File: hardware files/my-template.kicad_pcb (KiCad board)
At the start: 2 copper layers, 17.5 x 24.7 mm, 23 parts, among them IC1 AD8232ACPZ-R7, J1 Conn_01x09

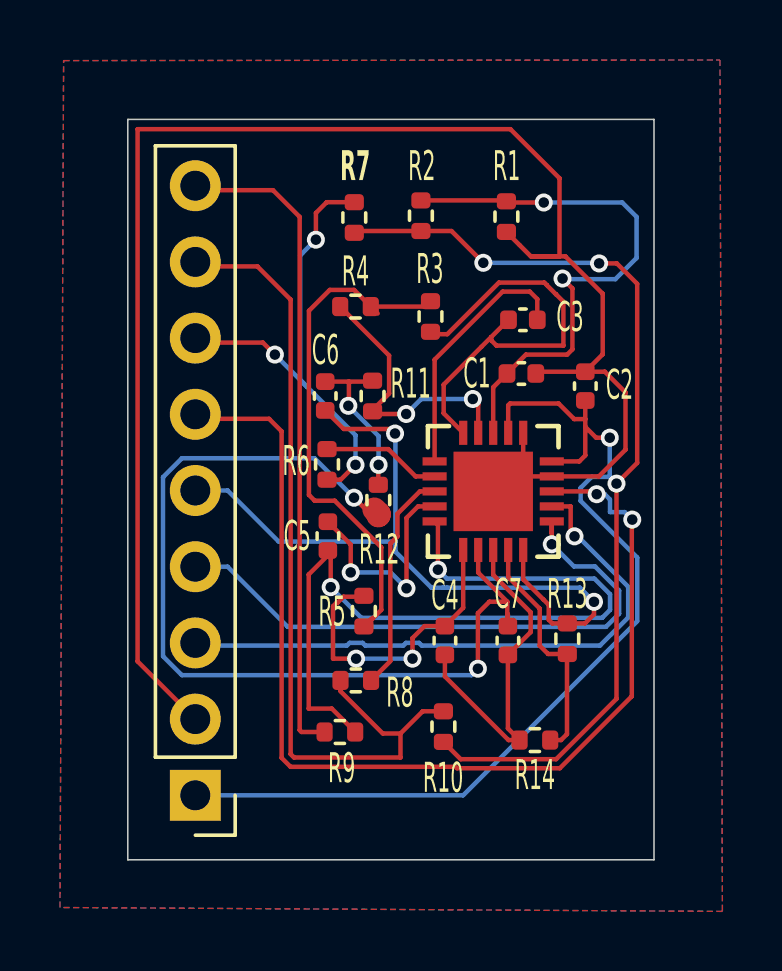
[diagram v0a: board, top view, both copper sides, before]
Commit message: update labels in pcb
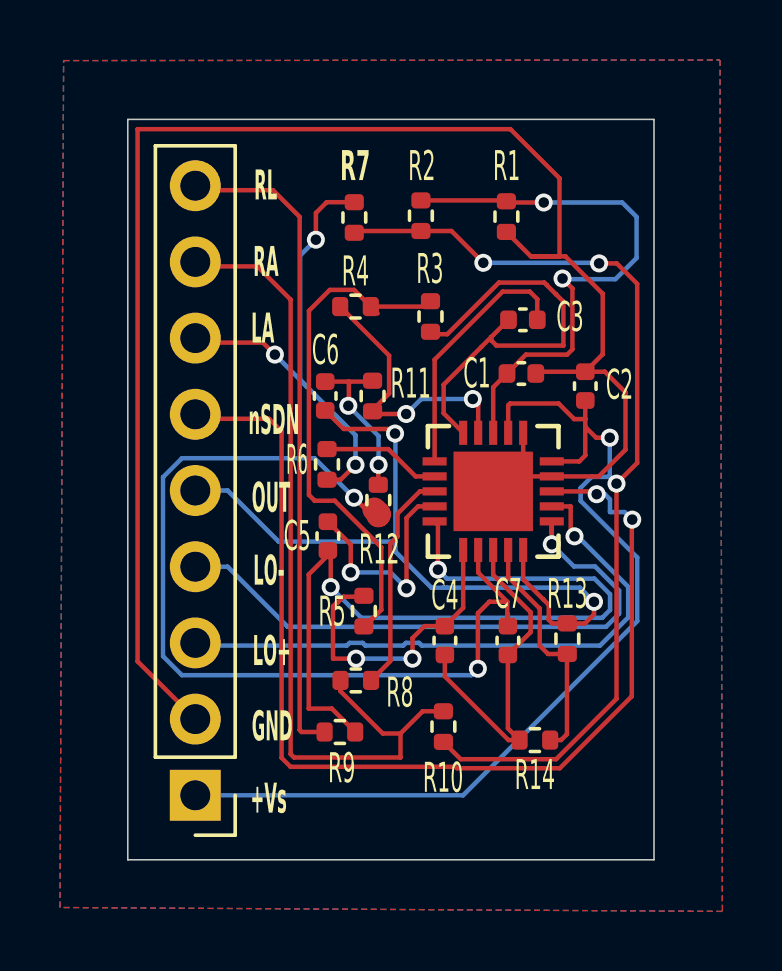
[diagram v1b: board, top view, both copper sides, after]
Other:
- board text added: "+Vs"
- board text added: "GND"
- board text added: "LA"
- board text added: "LO+"
- board text added: "LO-"
- board text added: "OUT"
- board text added: "RA"
- board text added: "RL"
- board text added: "nSDN"
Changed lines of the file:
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@@
 		(tags "resistor")
 		(property "Reference" "R6"
-			(at 0.11 -1.03 180)
+			(at 0.15 -1 180)
 			(layer "F.SilkS")
 			(effects
 				(font
-					(size 1 0.5)
+					(size 1 0.4)
 					(thickness 0.1)
 				)
@@
 		(layer "Edge.Cuts")
 	)
+	(gr_text "LO+"
+		(at 130.99 88.62 0)
+		(layer "F.SilkS")
+		(effects
+			(font
+				(size 1 0.4)
+				(thickness 0.1)
+				(bold yes)
+			)
+			(justify left bottom)
+		)
+	)
+	(gr_text "+Vs\n"
+		(at 130.92 93.54 0)
+		(layer "F.SilkS")
+		(effects
+			(font
+				(size 1 0.4)
+				(thickness 0.1)
+				(bold yes)
+			)
+			(justify left bottom)
+		)
+	)
+	(gr_text "RL"
+		(at 131.04 73.1 0)
+		(layer "F.SilkS")
+		(effects
+			(font
+				(size 1 0.4)
+				(thickness 0.1)
+				(bold yes)
+			)
+			(justify left bottom)
+		)
+	)
+	(gr_text "RA"
+		(at 131.01 75.65 0)
+		(layer "F.SilkS")
+		(effects
+			(font
+				(size 1 0.4)
+				(thickness 0.1)
+				(bold yes)
+			)
+			(justify left bottom)
+		)
+	)
+	(gr_text "nSDN\n"
+		(at 130.85 80.92 0)
+		(layer "F.SilkS")
+		(effects
+			(font
+				(size 1 0.4)
+				(thickness 0.1)
+				(bold yes)
+			)
+			(justify left bottom)
+		)
+	)
+	(gr_text "GND"
+		(at 130.96 91.13 0)
+		(layer "F.SilkS")
+		(effects
+			(font
+				(size 1 0.4)
+				(thickness 0.1)
+				(bold yes)
+			)
+			(justify left bottom)
+		)
+	)
+	(gr_text "OUT"
+		(at 130.96 83.51 0)
+		(layer "F.SilkS")
+		(effects
+			(font
+				(size 1 0.4)
+				(thickness 0.1)
+				(bold yes)
+			)
+			(justify left bottom)
+		)
+	)
+	(gr_text "LO-"
+		(at 131.01 85.94 0)
+		(layer "F.SilkS")
+		(effects
+			(font
+				(size 1 0.4)
+				(thickness 0.1)
+				(bold yes)
+			)
+			(justify left bottom)
+		)
+	)
+	(gr_text "LA\n"
+		(at 130.94 77.87 0)
+		(layer "F.SilkS")
+		(effects
+			(font
+				(size 1 0.4)
+				(thickness 0.1)
+				(bold yes)
+			)
+			(justify left bottom)
+		)
+	)
 	(dimension
 		(type orthogonal)
@@
 		(min_thickness 0.25)
 		(filled_areas_thickness no)
-		(fill
+		(fill yes
 			(thermal_gap 0.5)
 			(thermal_bridge_width 0.5)
